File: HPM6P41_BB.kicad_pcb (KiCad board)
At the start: 4 copper layers, 152.8 x 80.3 mm, 281 parts, among them J1 USB_B, J10 Conn_01x01, J11 Conn_01x01, J12 Conn_01x01, J2 USB_C_Receptacle_USB2.0_16P, J3 Conn_02x16_Odd_Even, J4 Conn_ARM_JTAG_SWD_20, J5 Conn_01x03, J6 Conn_01x03, J7 SMA, J8 SMA, J9 Conn_01x01, Q1 HYG080N10LS1C2, Q2 HYG080N10LS1C2, Q3 HYG080N10LS1C2, Q4 HYG080N10LS1C2, Q5 S8050, SW1 焊盘, SW2 Push_Button, SW3 Push_Button, SW4 Push_Button, U1 UCC27211ADRMR, U10 TJA1044GTK/3Z, U11 TPS54302, U12 LP5907MFX-3.3, U13 REF3030, U14 LM5164DDA, U15 SY8089, U16 INA241A3xDDF, U17 INA241A3xDDF, U18 UCC27519, U19 XC6206PxxxMR, U2 UCC27211ADRMR, U20 SGM8551XN, U21 SGM8551XN, U22 TMP112xxDRL, U3 UCC27519, U4 HPM6P41IPB1, U5 TPD4E05U06DQA, U6 AT24C08C-SSHM-T, U7 TMP112xxDRL, U8 TMP112xxDRL, U9 SIT3088ETK, Y1 24MHz ±10ppm 6pF

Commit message: 修复VDD_SOC的SNS未连接的错误
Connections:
- U4 pad 31: unconnected-(U4A-DCDC_SNS-Pad31) -> VDD_SOC
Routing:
- net VDD_SOC: track 16.4 -> 18.4 mm, vias 12 -> 13

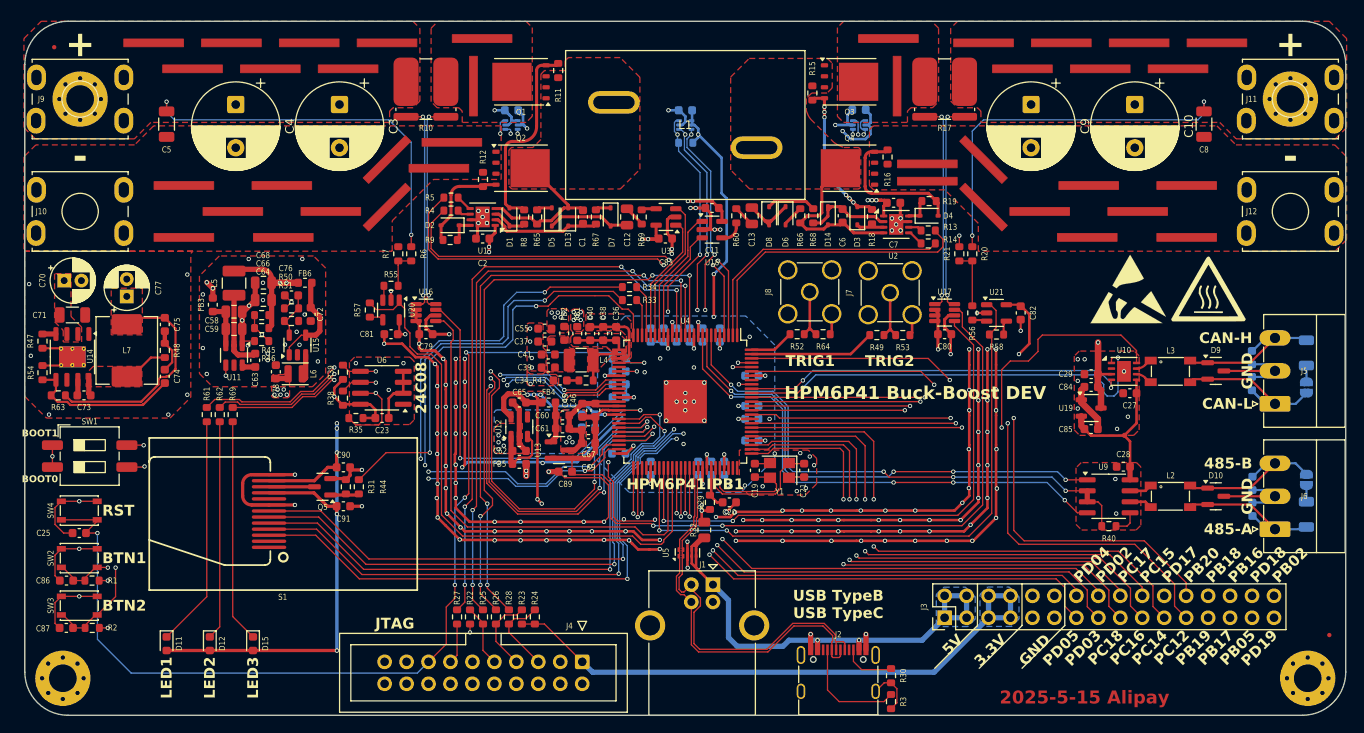
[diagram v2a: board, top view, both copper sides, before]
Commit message: 放置钳位二极管 修复分压器未接地
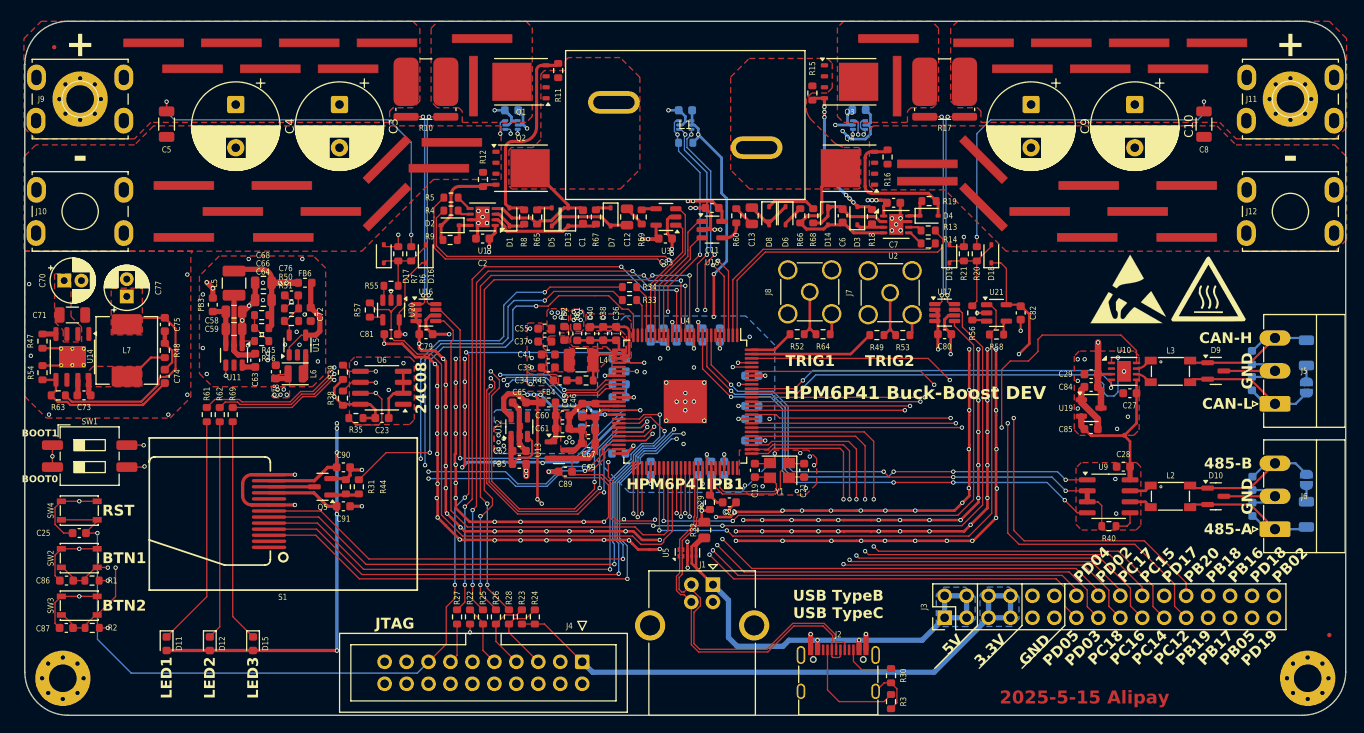
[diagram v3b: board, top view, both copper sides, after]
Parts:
- added D16: 1N4148WS, Diode_SMD:D_SOD-323, F.Cu at (120.0, 64.9)
- added D17: 1N4148WS, Diode_SMD:D_SOD-323, F.Cu at (115.1, 64.9)
- added D18: 1N4148WS, Diode_SMD:D_SOD-323, F.Cu at (185.4, 64.9)
- added D19: 1N4148WS, Diode_SMD:D_SOD-323, F.Cu at (180.6, 64.9)
- D1, D2, D3, D4, D5, D6, D7, D8: value 1N4148W -> 1N4148WS
- moved R20 0.53 mm to (183.7, 64.9)
- moved R21 0.53 mm to (182.2, 64.9)
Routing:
- net VANA: track 152.0 -> 166.3 mm
- net GND: track 592.1 -> 596.9 mm, vias 222 -> 223
- net /BB/OutputVsense+: track 6.73 -> 11.2 mm
- net /BB/InputVsense+: track 4.38 -> 8.72 mm
- net /PA13: track 47.9 -> 46.9 mm
- net /PA12: track 49.0 -> 48.0 mm
- net VOUT: track 43.5 -> 42.8 mm

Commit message: 交换LED与按键位置，优化布线，调整位号丝印
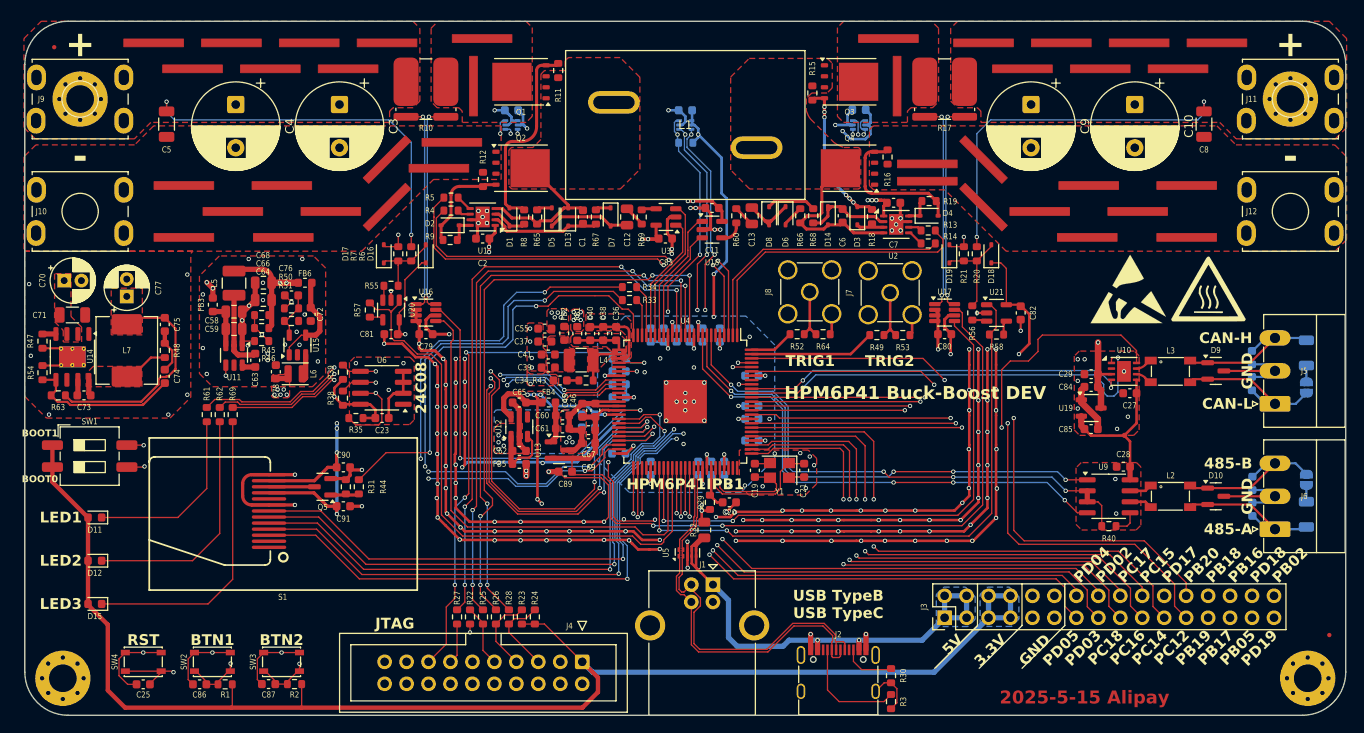
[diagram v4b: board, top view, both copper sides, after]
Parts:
- moved C87 24.3 mm to (101.8, 114.7)
- moved R2 24.3 mm to (104.8, 114.7)
- moved SW3 24.3 mm to (103.3, 112.1)
- moved C86 19.5 mm to (93.8, 114.7)
- moved R1 19.5 mm to (96.8, 114.7)
- moved SW2 19.5 mm to (95.3, 112.1)
- moved C25 19.0 mm to (87.3, 114.7)
- moved SW4 19.0 mm to (87.3, 112.1)
- moved D15 18.9 mm to (81.7, 105.4), turned to 180 degrees
- moved D11 16.8 mm to (81.7, 95.4), turned to 180 degrees
- moved D12 16.4 mm to (81.7, 100.4), turned to 180 degrees
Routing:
- net /MCU_MISC/RESETN: track 122.2 -> 99.7 mm
- net /PD20: track 83.7 -> 66.2 mm
- net Net-(D15-K): track 25.9 -> 34.6 mm
- net Net-(D11-K): track 26.8 -> 21.3 mm
- net /PD21: track 80.0 -> 74.5 mm
- net Net-(D12-K): track 25.4 -> 27.9 mm
- net +3.3V: track 373.8 -> 375.9 mm, vias 32 -> 28
- net /PB2: track 84.5 -> 83.8 mm

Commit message: 添加JTAG接口的ESD保护
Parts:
- added REF**: LayerMarker_4_6.35x2.54mm_TextH1mm_P1.27mm, Symbol:LayerMarker_4_6.35x2.54mm_TextH1mm_P1.27mm, F.Cu at (149.5, 118.3)
- added U23: TPD4E05U06DQA, Package_SON:USON-10_2.5x1.0mm_P0.5mm, F.Cu at (126.1, 70.9)
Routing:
- net GND: track 596.9 -> 599.5 mm, vias 223 -> 225
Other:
- board text added: "2025-5-22 Alipay Rev2"
- board text removed: "2025-5-15 Alipay"
